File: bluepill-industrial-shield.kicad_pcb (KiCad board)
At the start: 2 copper layers, 100 x 100 mm, 123 parts, among them J1 Conn_01x02_Socket, J2 Conn_01x16_Socket, J3 Conn_01x02_Socket, J4 Conn_01x12_Socket, Q1 BC817, Q10 BC817, Q11 BC817, Q12 BC817, Q13 BC817, Q14 BC817, Q2 BC817, Q3 BC817, Q4 BC817, Q5 BC817, Q6 BC817, Q7 BC817, Q8 BC817, Q9 BC817, U1 BluePill, U10 PC817, U11 PC817, U12 PC817, U13 PC817, U14 PC817, U15 PC817, U16 PC817, U17 PC817, U2 TMA-2405D, U20 PC817, U21 PC817, U22 PC817, U23 PC817, U24 PC817, U25 PC817, U26 PC817, U27 PC817, U28 PC817, U29 PC817, U3 MAX3485, U30 PC817, U31 PC817, U32 PC817, U33 PC817, U4 PC817, U5 PC817, U6 PC817, U7 PC817, U8 PC817, U9 PC817

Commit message: trace pcb
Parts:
- removed D13, D14: 1N4007, Diode_SMD:D_SMA_Handsoldering
- removed Q13, Q14: BC817, Package_TO_SOT_SMD:SOT-23
- removed the R41 at (137.0, 110.2)
- removed R42, R43, R44: 680, Resistor_SMD:R_0805_2012Metric_Pad1.20x1.40mm_HandSolder
- removed U32, U33: PC817, Package_DIP:DIP-4_W7.62mm
- added C15: 100nF, Capacitor_SMD:C_0805_2012Metric, F.Cu at (60.5, 134.2)
- added C16: 1nF, Capacitor_SMD:C_0805_2012Metric, F.Cu at (70.0, 133.7)
- added C17: C, Capacitor_SMD:C_0805_2012Metric, F.Cu at (63.2, 124.8)
- added J4: Conn_01x02_Socket, Connector_Phoenix_MC:PhoenixContact_MCV_1,5_2-G-3.5_1x02_P3.50mm_Vertical, F.Cu at (63.2, 145.1)
- added R15: 1K, Resistor_SMD:R_0805_2012Metric_Pad1.20x1.40mm_HandSolder, F.Cu at (63.2, 129.8)
- added R16: 2K, Resistor_SMD:R_0805_2012Metric_Pad1.20x1.40mm_HandSolder, F.Cu at (59.0, 129.8)
- added R17: 1K, Resistor_SMD:R_0805_2012Metric_Pad1.20x1.40mm_HandSolder, F.Cu at (63.2, 127.2)
- added U18: ACS712xLCTR-05B, Package_SO:SOIC-8_3.9x4.9mm_P1.27mm, F.Cu at (65.0, 135.8)
- J5: renamed from J4; footprint Connector_Phoenix_MC:PhoenixContact_MCV_1,5_14-G-3.5_1x14_P3.50mm_Vertical -> Connector_Phoenix_MC:PhoenixContact_MCV_1,5_12-G-3.5_1x12_P3.50mm_Vertical
- moved D1 35.0 mm to (89.5, 133.0)
- moved D2 33.2 mm to (94.5, 133.0)
- moved D3 31.2 mm to (99.2, 133.0), turned to -90 degrees
- moved D4 29.5 mm to (104.2, 133.0), turned to -90 degrees
- moved D5 27.7 mm to (109.2, 133.0), turned to -90 degrees
- moved D6 26.0 mm to (114.2, 133.0), turned to -90 degrees
- moved J5 24.5 mm to (98.0, 145.0)
- moved D7 24.2 mm to (119.2, 133.0), turned to -90 degrees
- moved D8 22.2 mm to (124.0, 133.0), turned to -90 degrees
- moved D9 20.5 mm to (129.0, 133.0), turned to -90 degrees
- moved D10 18.8 mm to (134.0, 133.0), turned to -90 degrees
- moved D11 17.0 mm to (139.0, 133.0), turned to -90 degrees
- moved Q1 15.3 mm to (69.8, 124.8)
- moved Q2 15.3 mm to (76.5, 124.8)
- moved R18 15.3 mm to (71.3, 110.5)
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- renumbered R17 to R18, R18 to R19, R19 to R20, R20 to R21, R21 to R22, R22 to R23, R23 to R24, R24 to R25, R25 to R26, R26 to R27, R27 to R28, R28 to R29, R29 to R30, R30 to R31, R31 to R32, R32 to R33, R33 to R34, R34 to R35, R35 to R36, R36 to R37, R37 to R38, R38 to R39, R39 to R40, R40 to R41, U20 to U19, U21 to U20, U22 to U21, U23 to U22, U24 to U23, U25 to U24, U26 to U25, U27 to U26, U28 to U27, U29 to U28, U30 to U29, U31 to U30
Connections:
- C1 pad 2: GND -> GND_IN
- C10 pad 2: GND -> GND_IN
- C11 pad 2: GND -> GND_IN
- C12 pad 2: GND -> GND_IN
- C13 pad 2: GND -> GND_IN
- C14 pad 2: GND -> GND_IN
- C2 pad 2: GND -> GND_IN
- C3 pad 2: GND -> GND_IN
- C4 pad 2: GND -> GND_IN
- C5 pad 2: GND -> GND_IN
- C6 pad 2: GND -> GND_IN
- C7 pad 2: GND -> GND_IN
- C8 pad 2: GND -> GND_IN
- C9 pad 2: GND -> GND_IN
- J1 pad 1: GND -> +24V
- J1 pad 2: +24V -> GND_IN
- Q1 pad 2: GND -> GND_IN
- Q10 pad 2: GND -> GND_IN
- Q11 pad 2: GND -> GND_IN
- Q12 pad 2: GND -> GND_IN
- Q2 pad 2: GND -> GND_IN
- Q3 pad 2: GND -> GND_IN
- Q4 pad 2: GND -> GND_IN
- Q5 pad 2: GND -> GND_IN
- Q6 pad 2: GND -> GND_IN
- Q7 pad 2: GND -> GND_IN
- Q8 pad 2: GND -> GND_IN
- Q9 pad 2: GND -> GND_IN
- U1 pad 10: /IN7 -> /IN6
- U1 pad 11: /IN6 -> /IN5
- U1 pad 12: /IN5 -> /I_SENS
- U1 pad 2: unconnected-(U1-PС13-Pad2) -> /IN12
- U1 pad 3: /IN14 -> unconnected-(U1-PС14-Pad3)
- U1 pad 36: /OUT13 -> /IN13
- U1 pad 37: /OUT14 -> /IN14
- U1 pad 4: /IN13 -> unconnected-(U1-PС15-Pad4)
- U1 pad 5: /IN12 -> /IN11
- U1 pad 6: /IN11 -> /IN10
- U1 pad 7: /IN10 -> /IN9
- U1 pad 8: /IN9 -> /IN8
- U1 pad 9: /IN8 -> /IN7
- U10 pad 2: GND -> GND_IN
- U11 pad 2: GND -> GND_IN
- U12 pad 2: GND -> GND_IN
- U13 pad 2: GND -> GND_IN
- U14 pad 2: GND -> GND_IN
- U15 pad 2: GND -> GND_IN
- U16 pad 2: GND -> GND_IN
- U17 pad 2: GND -> GND_IN
- U4 pad 2: GND -> GND_IN
- U5 pad 2: GND -> GND_IN
- U6 pad 2: GND -> GND_IN
- U7 pad 2: GND -> GND_IN
- U8 pad 2: GND -> GND_IN
- U9 pad 2: GND -> GND_IN
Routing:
- net +24V: track 0.00 -> 256.9 mm, vias 0 -> 24
- net +5V: track 0.00 -> 118.8 mm
- net +3.3V: track 0.00 -> 85.8 mm, vias 0 -> 1
- net /I_SENS: track 0.00 -> 60.6 mm
- net /TX: track 0.00 -> 58.9 mm, vias 0 -> 2
- net /RX: track 0.00 -> 57.9 mm, vias 0 -> 2
- net /TX_EN: track 0.00 -> 56.1 mm, vias 0 -> 2
- net /IN14: track 0.00 -> 38.6 mm
- net /DO2: track 0.00 -> 38.2 mm
- net /OUT12: track 0.00 -> 38.0 mm
- net /RS485_B: track 0.00 -> 37.5 mm
- net /DO1: track 0.00 -> 37.5 mm
- net /RS485_A: track 0.00 -> 36.0 mm
- net /DO3: track 0.00 -> 35.7 mm
- net /IN13: track 0.00 -> 34.5 mm
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- added copper zone on B.Cu, net GND
- added copper zone on F.Cu, net GND
- added copper zone on B.Cu, net GND_IN
- added copper zone on F.Cu, net GND_IN

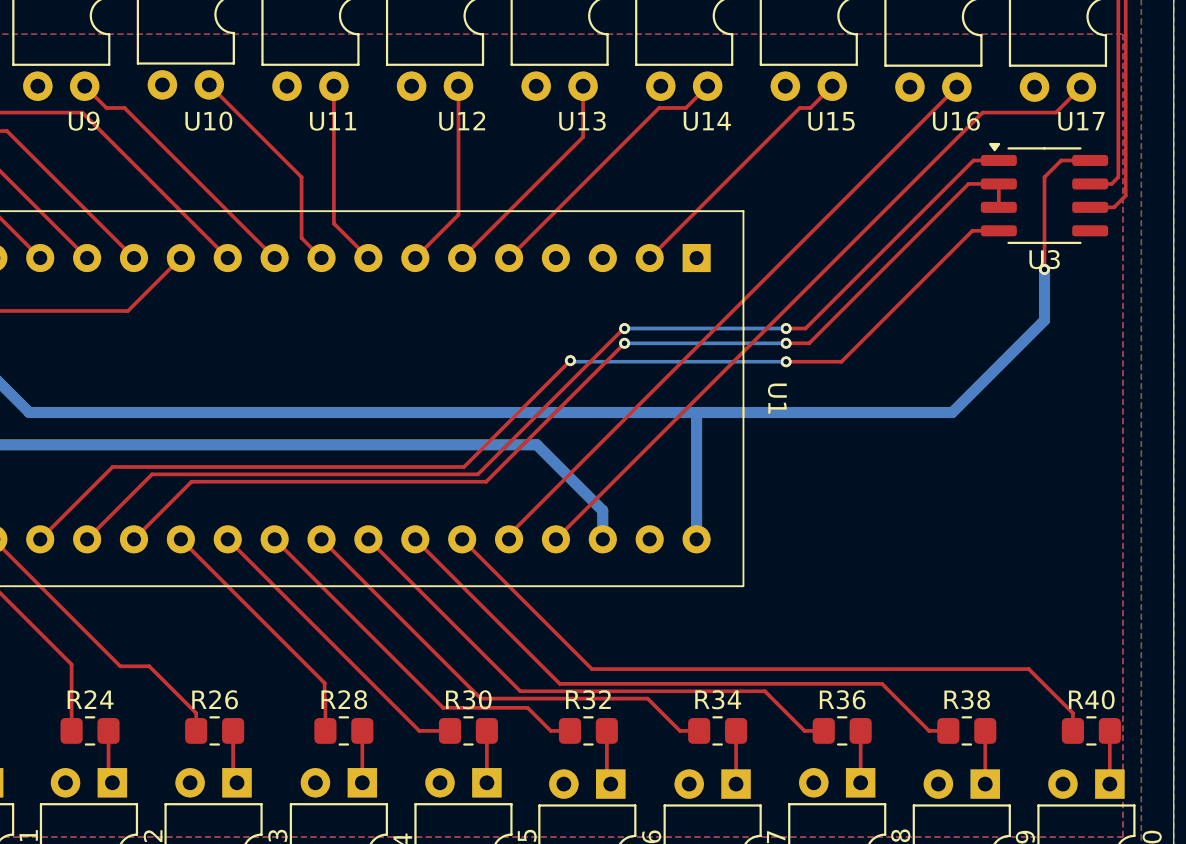
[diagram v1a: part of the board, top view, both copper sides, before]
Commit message: add battery
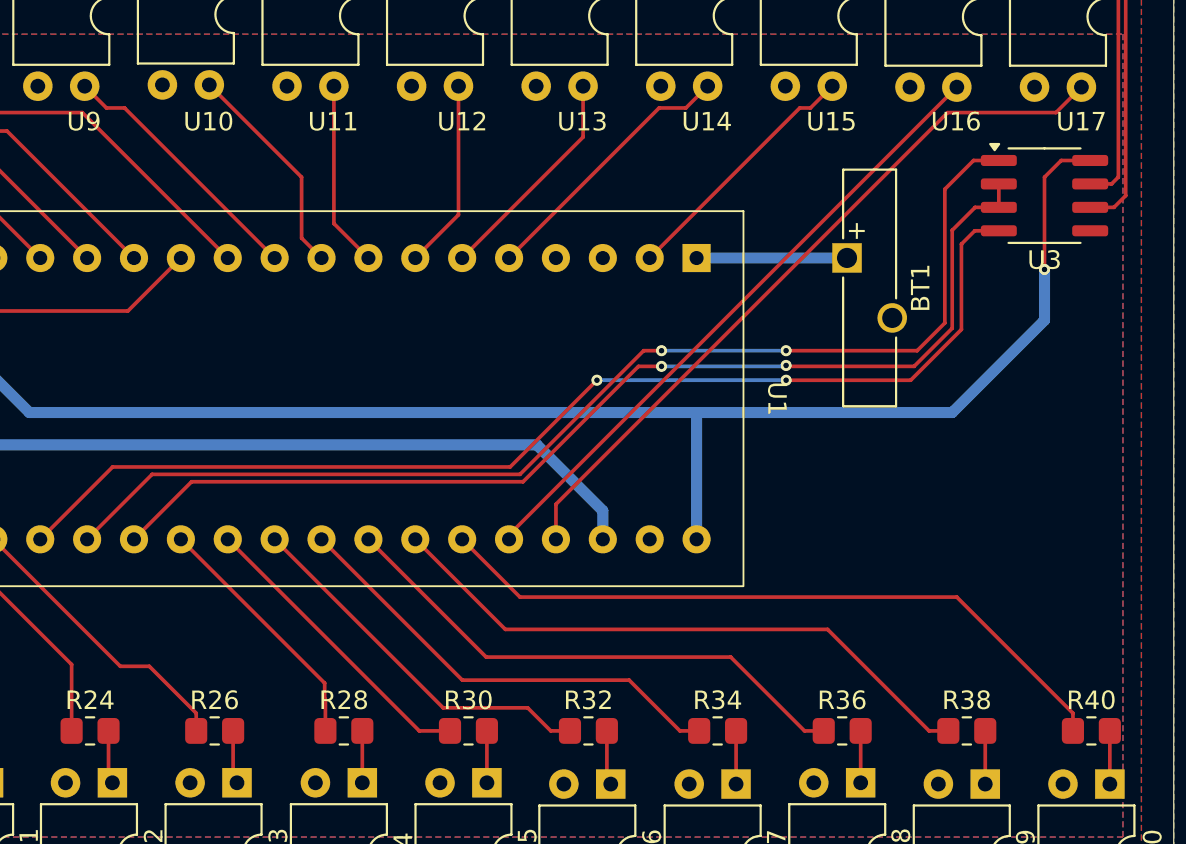
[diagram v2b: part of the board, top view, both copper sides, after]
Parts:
- added BT1: Battery_Cell, Battery:Battery_Panasonic_CR1220-VCN_Vertical_CircularHoles, F.Cu at (132.3, 84.9)
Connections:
- U1 pad 1: unconnected-(U1-VBAT-Pad1) -> +BATT
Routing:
- net +BATT: track 0.00 -> 8.15 mm
- net /RX: track 57.9 -> 62.1 mm
- net /TX_EN: track 56.1 -> 59.1 mm
- net /TX: track 58.9 -> 61.6 mm
- net /IN14: track 38.6 -> 39.7 mm

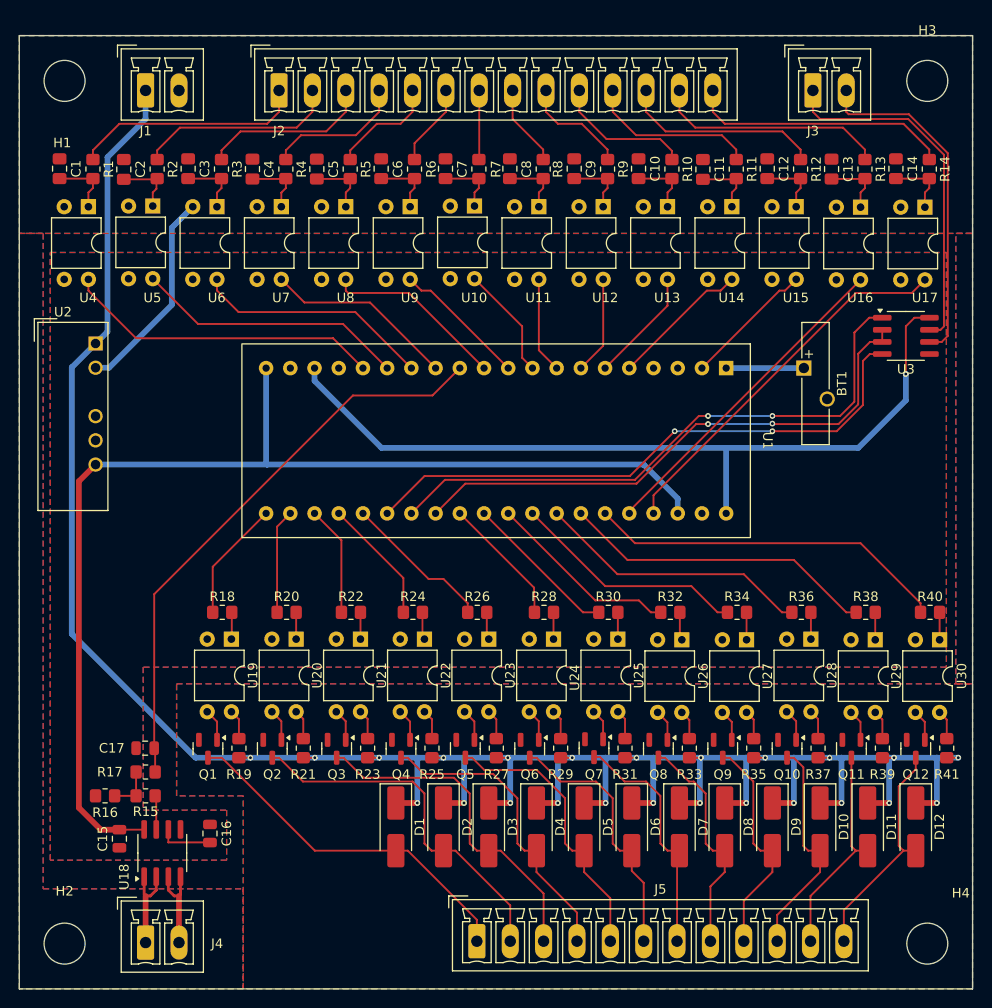
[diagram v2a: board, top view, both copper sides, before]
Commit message: update to kicad 9
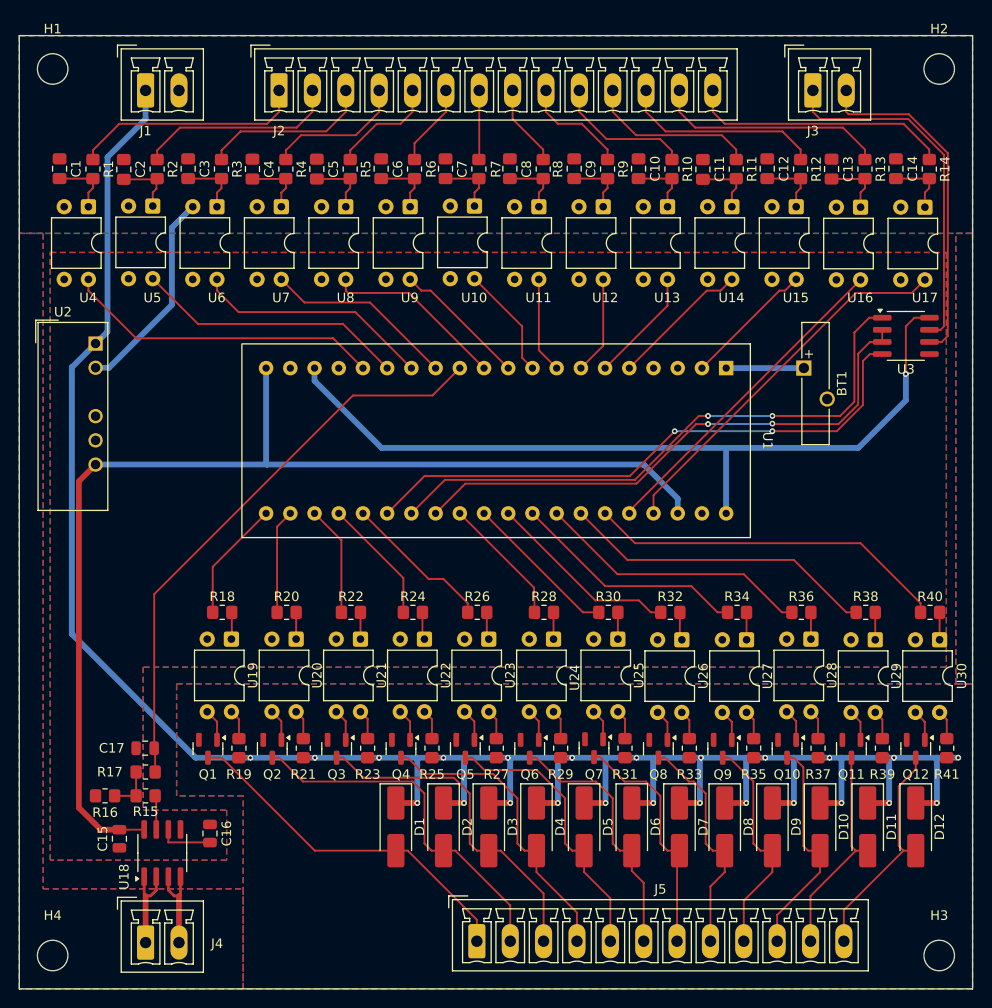
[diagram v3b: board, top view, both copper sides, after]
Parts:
- H1, H2, H3, H4: footprint MountingHole:MountingHole_4.3mm_M4 -> MountingHole:MountingHole_3.2mm_M3
- moved H2 129.8 mm to (146.5, 53.5)
- moved H3 91.8 mm to (146.5, 146.5)
- moved H4 91.8 mm to (53.5, 146.5)
- moved H1 1.77 mm to (53.5, 53.5)
